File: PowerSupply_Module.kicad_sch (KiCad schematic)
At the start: 40 parts, among them J6 Conn_01x02_Socket, J7 Conn_01x02_Socket, U12 MP2637AGR-P, U13 MC34063AD

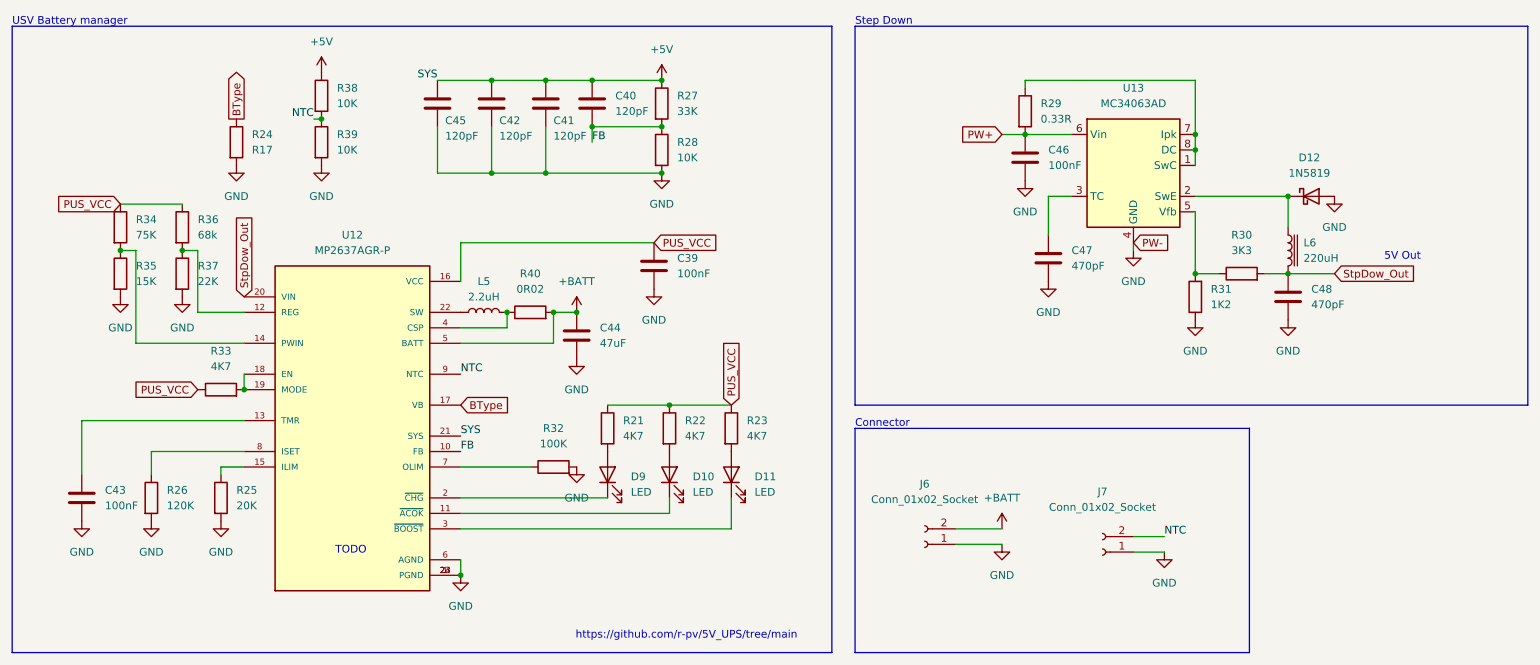
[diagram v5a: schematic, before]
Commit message: cleaned up scematics and updated power management
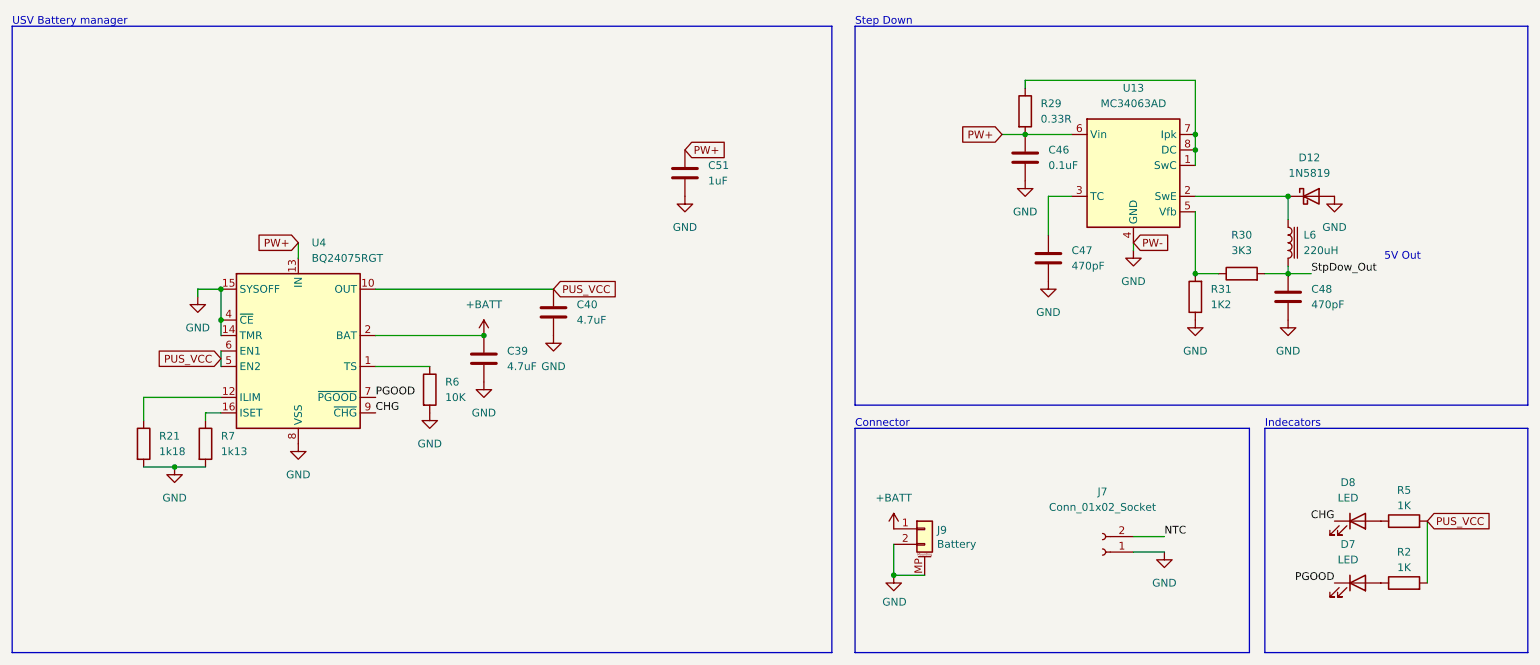
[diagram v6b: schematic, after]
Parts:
- removed C41, C42, C45: 120pF, symbol Device:C
- removed C43: 100nF, symbol Device:C
- removed C44: 47uF, symbol Device:C
- removed D10, D11, D9: LED, Capacitor_SMD:C_0603_1608Metric, symbol Device:LED
- removed J6: Conn_01x02_Socket, Connector_PinHeader_1.00mm:PinHeader_1x02_P1.00mm_Vertical, symbol Connector:Conn_01x02_Socket
- removed L5: 2.2uH, Inductor_SMD:L_Bourns_SRP7028A_7.3x6.6mm, symbol Device:L
- removed R22, R23, R33: 4K7, Resistor_SMD:R_0603_1608Metric, symbol Device:R
- removed R24: R17, Resistor_SMD:R_0603_1608Metric, symbol Device:R
- removed R25: 20K, Resistor_SMD:R_0603_1608Metric, symbol Device:R
- removed R26: 120K, Resistor_SMD:R_0603_1608Metric, symbol Device:R
- removed R27: 33K, Resistor_SMD:R_0603_1608Metric, symbol Device:R
- removed R28, R38, R39: 10K, Resistor_SMD:R_0603_1608Metric, symbol Device:R
- removed R32: 100K, Resistor_SMD:R_0603_1608Metric, symbol Device:R
- removed R34: 75K, Resistor_SMD:R_0603_1608Metric, symbol Device:R
- removed R35: 15K, Resistor_SMD:R_0603_1608Metric, symbol Device:R
- removed R36: 68k, Resistor_SMD:R_0603_1608Metric, symbol Device:R
- removed R37: 22K, Resistor_SMD:R_0603_1608Metric, symbol Device:R
- removed R40: 0R02, Resistor_SMD:R_0603_1608Metric, symbol Device:R
- removed U12: MP2637AGR-P, MP2637AGR-P:IC_MP2637AGR-P, symbol MP2637AGR-P:MP2637AGR-P
- added C51: 1uF, Capacitor_SMD:C_0603_1608Metric, symbol Device:C
- added D7, D8: LED, Capacitor_SMD:C_0603_1608Metric, symbol Device:LED
- added J9: Battery, Connector_JST:JST_PH_S2B-PH-SM4-TB_1x02-1MP_P2.00mm_Horizontal, symbol Connector_Generic_MountingPin:Conn_01x02_MountingPin
- added R2, R5: 1K, Resistor_SMD:R_0603_1608Metric, symbol Device:R
- added R6: 10K, Resistor_SMD:R_0603_1608Metric, symbol Device:R
- added R7: 1k13, Resistor_SMD:R_0603_1608Metric, symbol Device:R
- added U4: BQ24075RGT, Package_DFN_QFN:VQFN-16-1EP_3x3mm_P0.5mm_EP1.6x1.6mm, symbol Battery_Management:BQ24075RGT
- C39: value 100nF -> 4.7uF; footprint (none) -> Capacitor_SMD:C_0805_2012Metric
- C40: value 120pF -> 4.7uF; footprint (none) -> Capacitor_SMD:C_0805_2012Metric
- C46: value 100nF -> 0.1uF; footprint (none) -> Capacitor_SMD:C_0805_2012Metric
- C47, C48: footprint (none) -> Capacitor_SMD:C_0603_1608Metric
- R21: value 4K7 -> 1k18
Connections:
- net +5V is gone; now on net PUS_VCC: C40.1
- net FB is gone; now on net GND: C40.2
- net +BATT: now also C39.1, J9.1 (Pin_1), U4.2 (BAT), U4.3 (BAT)
- net GND: now also R21.2, C51.2, J9.2 (Pin_2), J9.MP (MountPin), R6.2, R7.2, U4.14 (TMR), U4.15 (SYSOFF), U4.17 (VSS), U4.4 (~{CE}), U4.8 (VSS)
- net PUS_VCC: now also R2.2, R5.2, U4.10 (OUT), U4.11 (OUT), U4.5 (EN2), U4.6 (EN1); no longer C39.1, R21.1
- net PW+: now also C51.1, U4.13 (IN)
- new net: R21.1, U4.12 (ILIM)
- new net: D7.2 (A), R2.1
- new net: R6.1, U4.1 (TS)
- new net: R7.1, U4.16 (ISET)
- new net: D8.2 (A), R5.1
- new net CHG: D8.1 (K), U4.9 (~{CHG})
- new net PGOOD: D7.1 (K), U4.7 (~{PGOOD})
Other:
- note added: "Indecators"
- note removed: "TODO"
- note removed: "https://github.com/r-pv/5V_UPS/tree/main"
- moved on the sheet: L6

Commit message: finelized scematics
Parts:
- removed J7: Conn_01x02_Socket, Connector_PinHeader_1.00mm:PinHeader_1x02_P1.00mm_Vertical, symbol Connector:Conn_01x02_Socket
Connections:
- net PUS_VCC renamed +5V
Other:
- moved on the sheet: J9

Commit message: mostly layouted
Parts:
- D12: footprint Diode_THT:D_DO-41_SOD81_P10.16mm_Horizontal -> Diode_SMD:D_SOD-123
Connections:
- net PW+: no longer C51.1, U4.13 (IN)
- net StpDow_Out: now also C51.1, U4.13 (IN)
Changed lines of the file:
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@@
 	)
 	(label "StpDow_Out"
-		(at 228.6 57.15 0)
+		(at 125.73 36.83 180)
 		(fields_autoplaced yes)
 		(effects
@@
 				(size 1.27 1.27)
 			)
-			(justify left bottom)
-		)
-	)
-	(label "CHG"
-		(at 232.41 97.79 180)
+			(justify right bottom)
+		)
+	)
+	(label "StpDow_Out"
+		(at 228.6 57.15 0)
 		(fields_autoplaced yes)
 		(effects
@@
 				(size 1.27 1.27)
 			)
-			(justify right bottom)
-		)
-	)
-	(global_label "PW+"
-		(shape input)
-		(at 125.73 36.83 0)
+			(justify left bottom)
+		)
+	)
+	(label "StpDow_Out"
+		(at 62.23 52.07 180)
 		(fields_autoplaced yes)
 		(effects
@@
 				(size 1.27 1.27)
 			)
-			(justify left)
-		)
-		(property "Intersheetrefs" "${INTERSHEET_REFS}"
-			(at 133.009 36.83 0)
-			(effects
-				(font
-					(size 1.27 1.27)
-				)
-				(justify left)
-				(hide yes)
-			)
+			(justify right bottom)
+		)
+	)
+	(label "CHG"
+		(at 232.41 97.79 180)
+		(fields_autoplaced yes)
+		(effects
+			(font
+				(size 1.27 1.27)
+			)
+			(justify right bottom)
 		)
 	)
@@
 		(property "Intersheetrefs" "${INTERSHEET_REFS}"
 			(at 170.521 34.29 0)
-			(effects
-				(font
-					(size 1.27 1.27)
-				)
-				(justify right)
-				(hide yes)
-			)
-		)
-	)
-	(global_label "PW+"
-		(shape input)
-		(at 62.23 52.07 180)
-		(fields_autoplaced yes)
-		(effects
-			(font
-				(size 1.27 1.27)
-			)
-			(justify right)
-		)
-		(property "Intersheetrefs" "${INTERSHEET_REFS}"
-			(at 54.951 52.07 0)
 			(effects
 				(font
@@
 			)
 		)
-		(property "Footprint" "Diode_THT:D_DO-41_SOD81_P10.16mm_Horizontal"
+		(property "Footprint" "Diode_SMD:D_SOD-123"
 			(at 228.6 48.895 0)
 			(effects
